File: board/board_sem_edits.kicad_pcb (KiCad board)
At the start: 2 copper layers, 92 x 75.8 mm, 68 parts, among them J2 Conn_01x01, J3 Conn_01x01, J3 Conn_01x25_Socket, J4 Conn_01x01, J4 Conn_01x25_Socket, J5 Conn_01x01, J5 PJ-320B, J6 Screw_Terminal_01x02, J7 Screw_Terminal_01x02, J8 Screw_Terminal_01x02

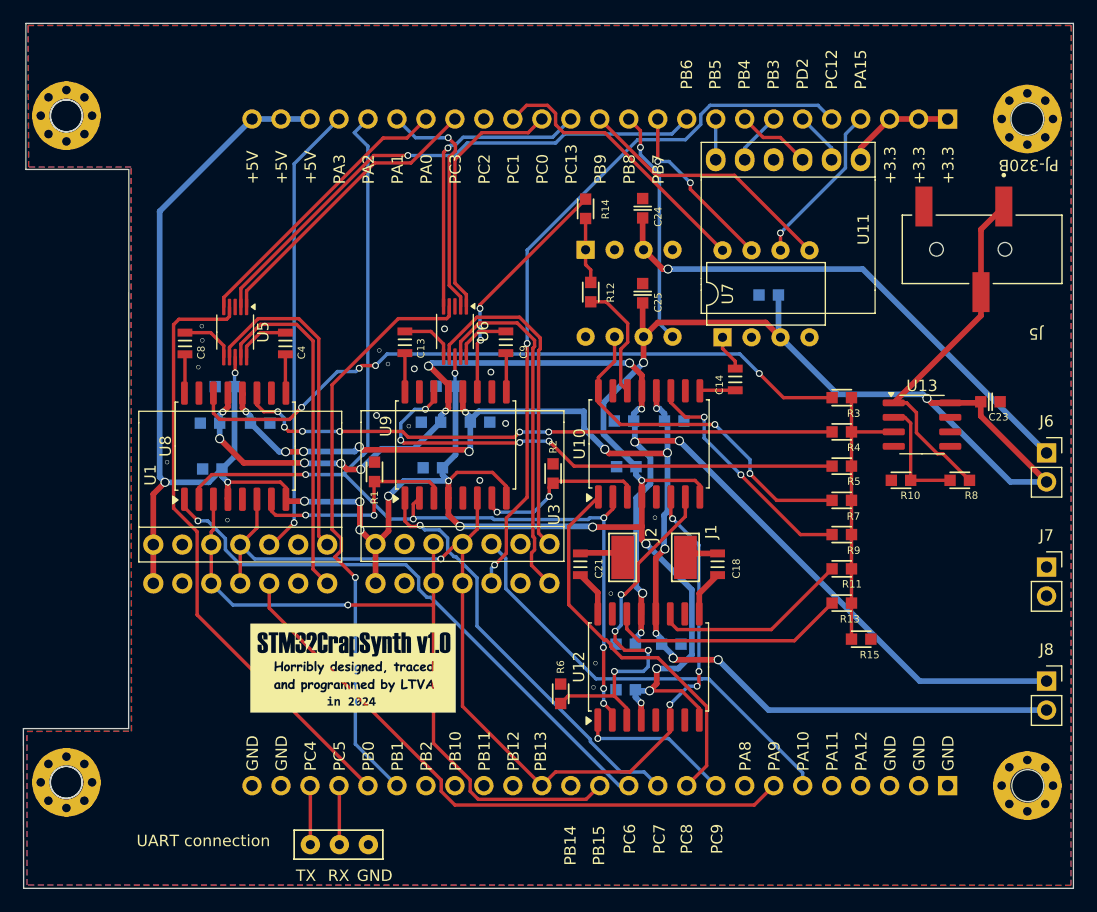
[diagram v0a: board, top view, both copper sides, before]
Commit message: fix uart comms, place interrupt handlers in ccmram, AD9833 works
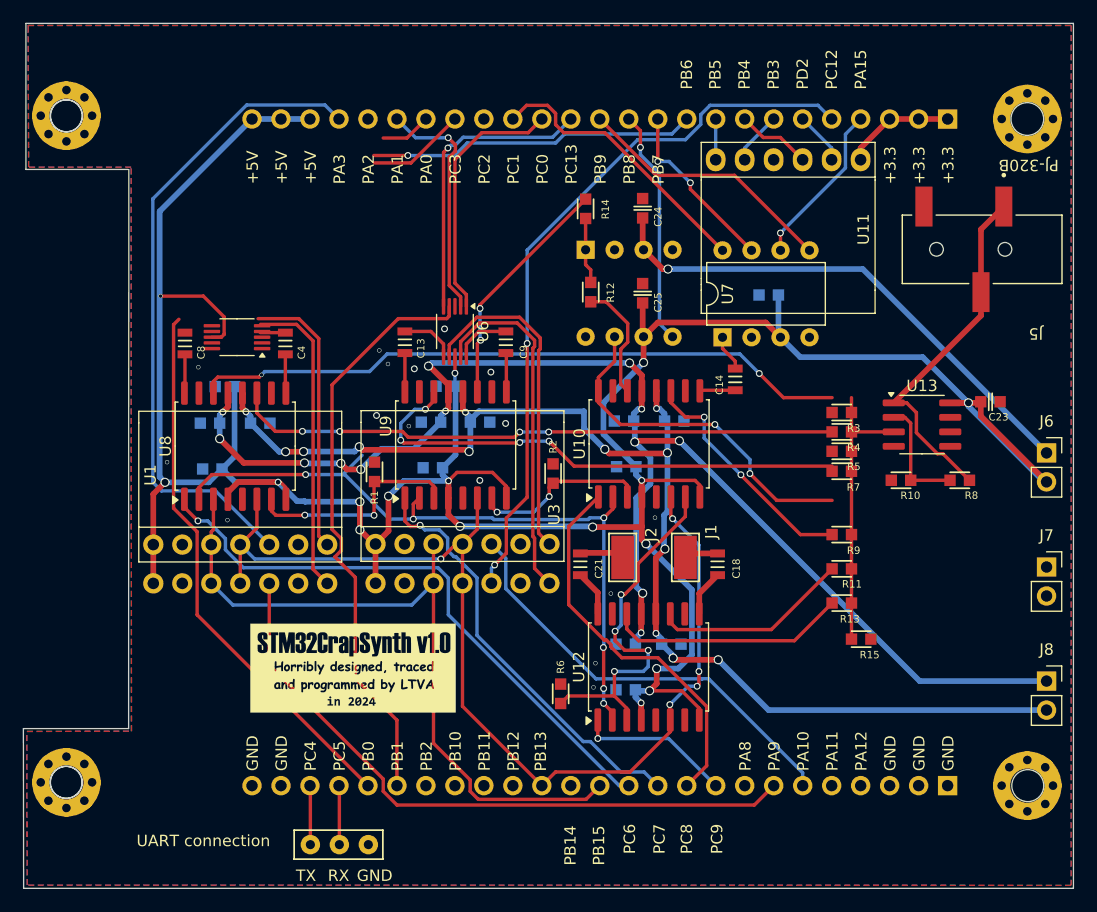
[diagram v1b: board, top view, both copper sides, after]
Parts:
- moved R7 2.55 mm to (169.7, 84.5)
- moved R3 1.30 mm to (169.7, 79.3)
- moved R5 1.30 mm to (169.7, 82.7)
- moved U5 0.48 mm to (116.7, 72.7), turned to 180 degrees
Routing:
- net ATTEN_CS: track 94.2 -> 63.4 mm
- net MUX_SEL_2: track 25.0 -> 4.43 mm
- net PWM2: track 46.8 -> 28.7 mm
- net CS_AD9833_1: track 40.0 -> 57.8 mm, vias 1 -> 0
- net MUX_SEL_1: track 25.9 -> 8.64 mm
- net +5V: track 256.1 -> 265.8 mm, vias 18 -> 17
- net PWM1: track 53.5 -> 48.1 mm
- net CH1_TOVOL: track 4.88 -> 0.00 mm
- net DDS1_out: track 28.8 -> 24.4 mm
- net DDS2_out: track 30.6 -> 27.0 mm
- net CS_AD9833_2: track 54.8 -> 57.8 mm
- net CH2_TOVOL: track 4.85 -> 2.20 mm
- net CH1_OUT: track 60.2 -> 57.8 mm, vias 4 -> 2
- net ZCEN_1: track 50.9 -> 52.2 mm
- net Analog_data: track 62.9 -> 63.7 mm, vias 1 -> 0
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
